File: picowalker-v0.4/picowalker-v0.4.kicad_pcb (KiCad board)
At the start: 4 copper layers, 47.4 x 50.5 mm, 105 parts, among them J1 12402012E212A, J2 BAT, J3 SWD, J4 UART, SW1 ~{BOOT}, SW2 RUN, SW3 BUT_M, SW4 BUT_R, SW5 BUT_L, U1 RP2350A-QFN60, U2 W25Q128JVP, U3 BMA400, U4 M95512DxMC, U5 TFBS4711, U6 BQ25628ERYKR, U7 DO0180FMST0x, U8 DT1240-04LP-7, U9 RT6150B-33GQW, Y1 ABM8-272-T3, Y2 SIT1533AI-H4-DCC-32.768E

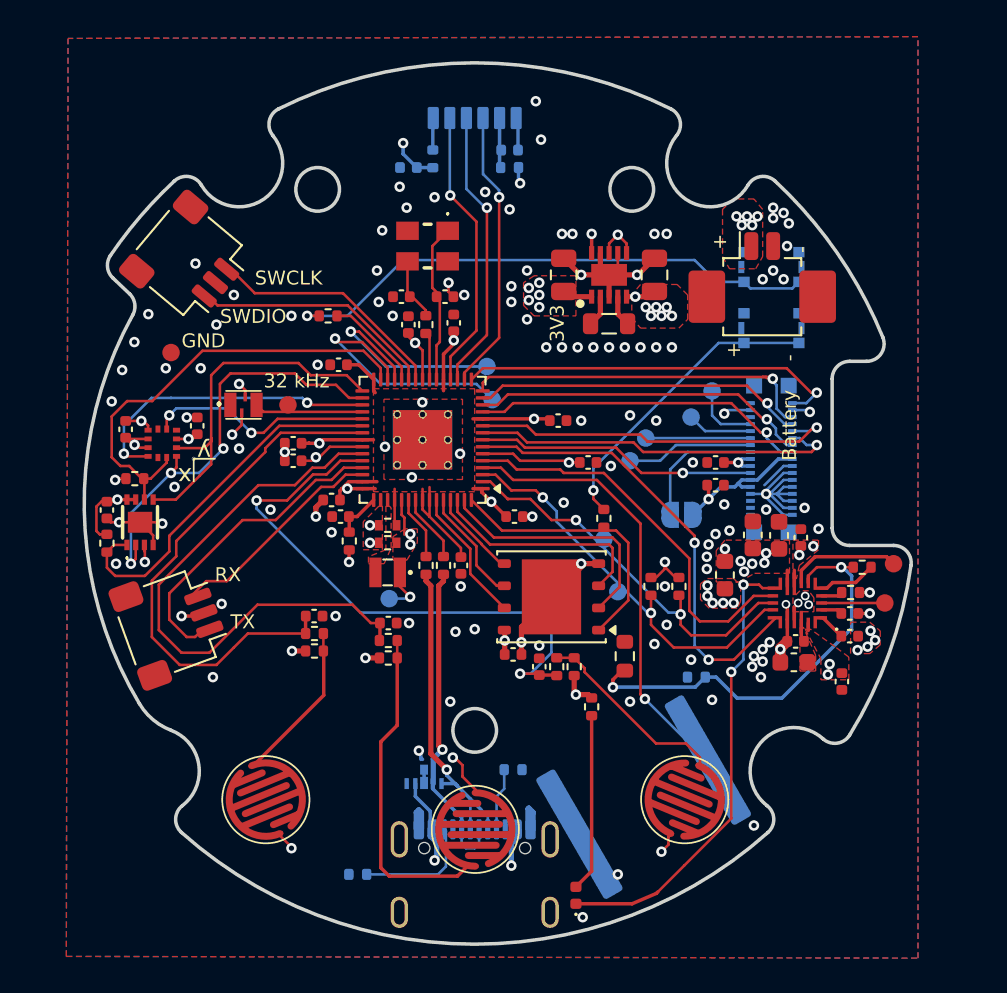
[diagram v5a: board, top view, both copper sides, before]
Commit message: v0.4: connect i2c to TP and add silkscreen labels
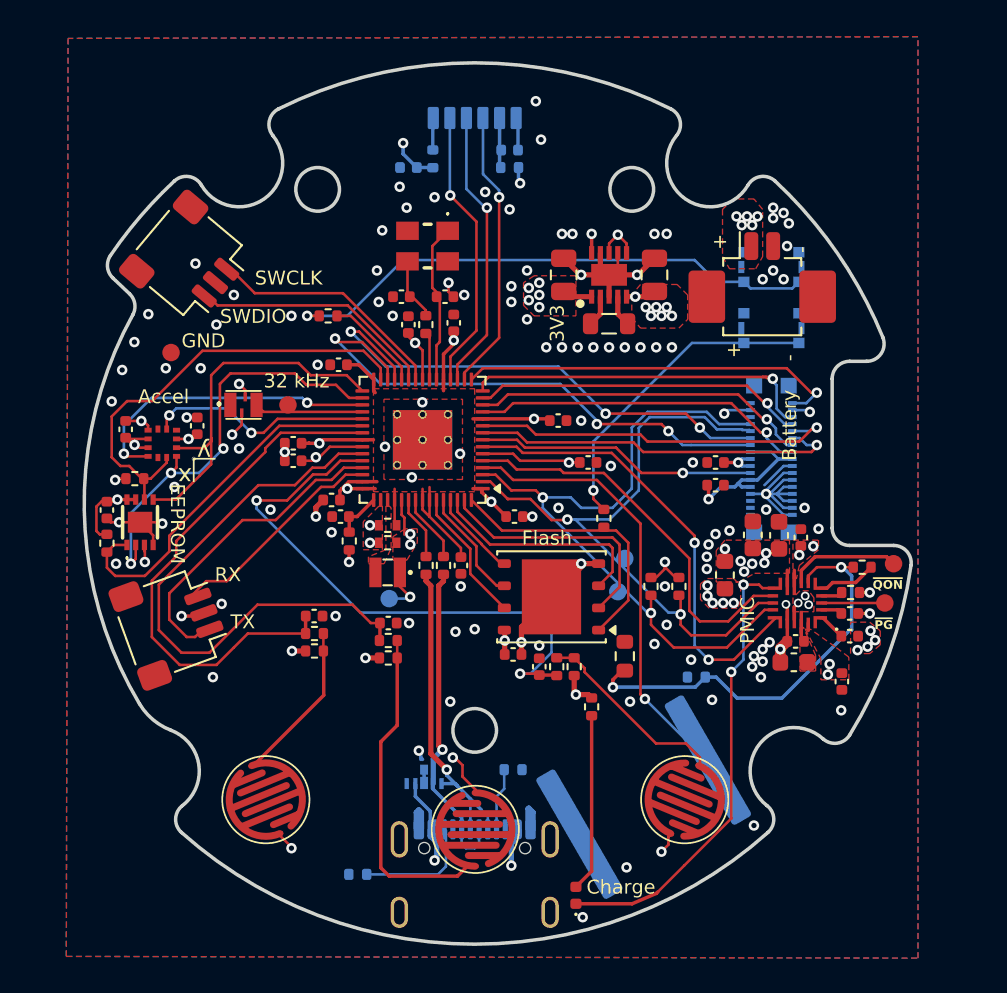
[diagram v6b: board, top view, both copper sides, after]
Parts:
- removed JP1: TP_VCC_JMP, Jumper:SolderJumper-2_P1.3mm_Open_RoundedPad1.0x1.5mm
- removed TP10: TP_SCL, picowalker:TestPoint_Pad_D1.0mm_Nosilk
- removed TP11: TP_SDA, picowalker:TestPoint_Pad_D1.0mm_Nosilk
- removed TP6: GP16, picowalker:TestPoint_Pad_D1.0mm_Nosilk
- removed TP7: GP17, picowalker:TestPoint_Pad_D1.0mm_Nosilk
- removed TP8: TP_INT, picowalker:TestPoint_Pad_D1.0mm_Nosilk
- removed TP9: TP_RESET, picowalker:TestPoint_Pad_D1.0mm_Nosilk
- moved TP5 1.63 mm to (158.6, 102.9)
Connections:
- U1 pad 27: /mcu/GP16 -> /TP_INT
- U1 pad 28: /mcu/GP17 -> /TP_RESET
- U7 pad 10: /screen/TP_I2C.SDA -> /mcu/I2C.SDA
- U7 pad 16: /screen/TP_VCC -> +3.3V
- U7 pad 8: /screen/TP_I2C.SCL -> /mcu/I2C.SCL
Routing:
- net /TP_RESET: track 7.27 -> 30.9 mm, vias 0 -> 3
- net /TP_INT: track 6.00 -> 29.5 mm, vias 0 -> 3
- net /mcu/I2C.SCL: track 23.4 -> 40.2 mm
- net /mcu/I2C.SDA: track 22.5 -> 37.5 mm
- net /mcu/GP17: track 14.9 -> 0.00 mm, vias 1 -> 0
- net /mcu/GP16: track 12.7 -> 0.00 mm, vias 1 -> 0
- net /screen/TP_VCC: track 7.61 -> 0.00 mm
- net /screen/TP_I2C.SCL: track 3.81 -> 0.00 mm
- net /screen/TP_I2C.SDA: track 3.73 -> 0.00 mm
- net /mcu/~{BOOT}: track 17.4 -> 18.3 mm
- net GND: vias 120 -> 118
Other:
- board text added: "=)"
- board text added: "Accel"
- board text added: "Charge"
- board text added: "EEPROM"
- board text added: "Flash"
- board text added: "Good luck!"
- board text added: "IRDA"
- board text added: "PMIC"
- board text added: "~{PG}"
- board text added: "~{QON}"
- board text removed: "GP16"
- board text removed: "GP17"
- board text removed: "TP_INT"
- board text removed: "TP_RESET"
- board text removed: "TP_SCL"
- board text removed: "TP_SDA"
- board text removed: "TP_VCC"
